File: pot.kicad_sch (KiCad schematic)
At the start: 8 parts, among them U25 LUM-1502-03_3.5mm_mono_vertic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, U26 LM358

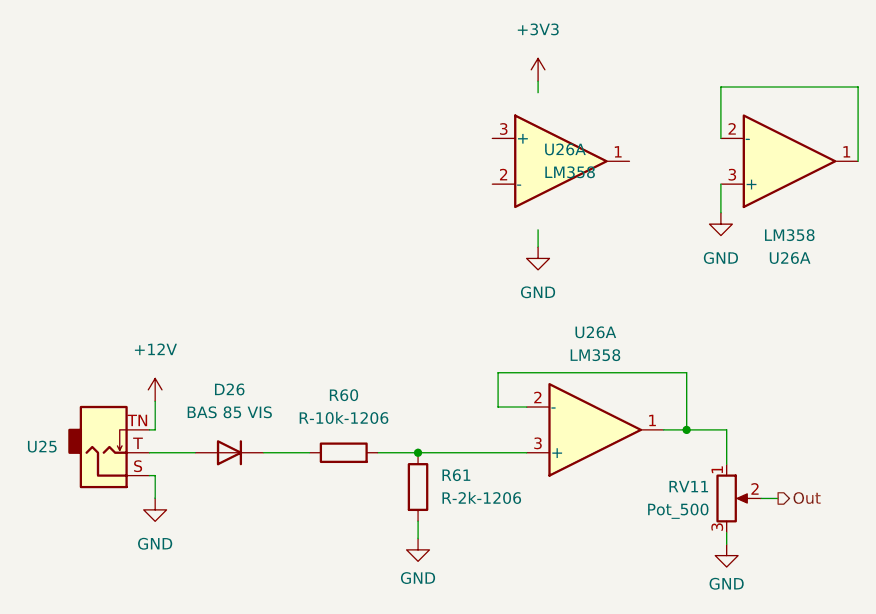
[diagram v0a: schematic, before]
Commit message: re-thinked the controls
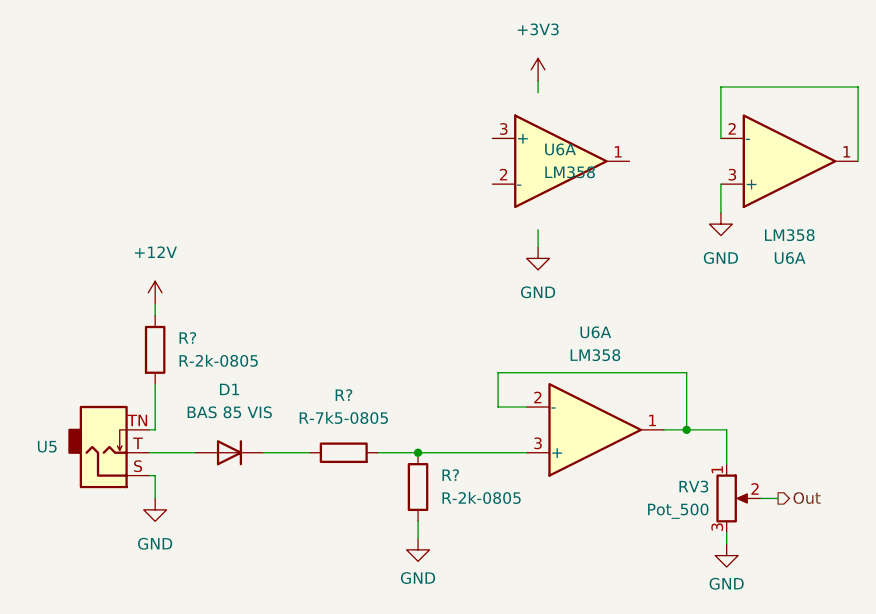
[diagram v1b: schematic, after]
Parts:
- removed R60: R-10k-1206, Resistor_SMD:R_1206_3216Metric_Pad1.30x1.75mm_HandSolder, symbol eurorack:R-10k-1206
- removed R61: R-2k-1206, Resistor_SMD:R_1206_3216Metric_Pad1.30x1.75mm_HandSolder, symbol eurorack:R-2k-1206
- added R? (x2): R-2k-0805, Resistor_SMD:R_0805_2012Metric, symbol eurorack:R-2k-0805
- added R?: R-7k5-0805, Resistor_SMD:R_0805_2012Metric, symbol eurorack:R-7k5-0805
- renumbered D26 to D1, RV11 to RV3, U25 to U5, U26 to U6
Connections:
- net +12V: now also R?.1; no longer U5.TN
- net GND: now also R?.2
- net at D1.2 (K): now also R?.1
- net at U6.3 (+): now also R?.1, R?.2
- new net: R?.2, U5.TN

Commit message: added some missing wires, whoopppssssz
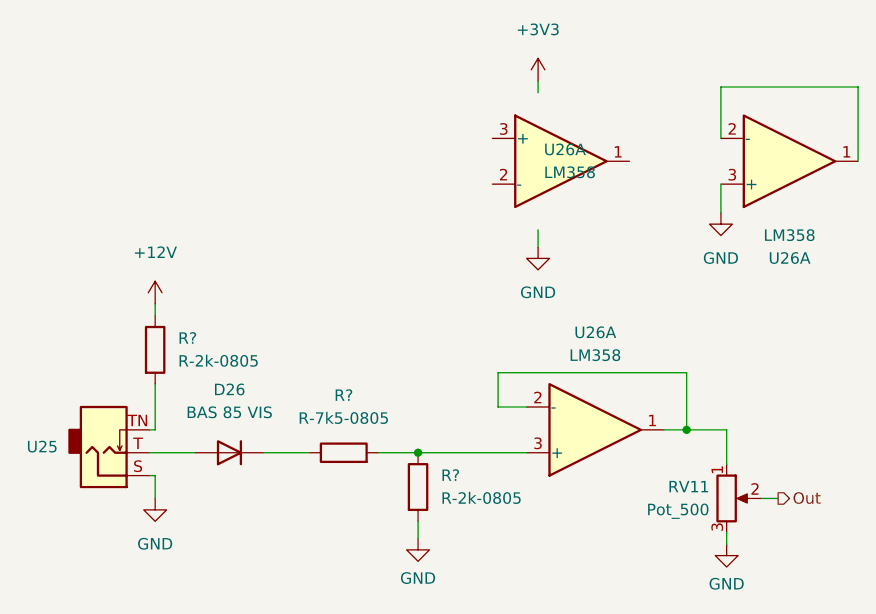
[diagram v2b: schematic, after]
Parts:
- renumbered D1 to D26, RV3 to RV11, U5 to U25, U6 to U26
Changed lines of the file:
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@@
+    (stroke (width 0) (type default) (color 0 0 0 0))
+  )
+  (wire (pts (xy 98.425 63.5) (xy 102.87 63.5))
+    (stroke (width 0) (type default) (color 0 0 0 0))
+  )
+  (wire (pts (xy 39.37 68.58) (xy 38.735 68.58))
+    (stroke (width 0) (type default) (color 0 0 0 0))
+  )
+  (wire (pts (xy 98.425 63.5) (xy 95.885 63.5))
+    (stroke (width 0) (type default) (color 0 0 0 0))
+  )
+  (wire (pts (xy 102.87 74.93) (xy 102.87 76.2))
+    (stroke (width 0) (type default) (color 0 0 0 0))
+  )
+  (wire (pts (xy 68.58 66.04) (xy 80.645 66.04))
+    (stroke (width 0) (type default) (color 0 0 0 0))
+  )
+  (wire (pts (xy 81.915 24.765) (xy 81.915 26.035))
+    (stroke (width 0) (type default) (color 0 0 0 0))
+  )
+  (wire (pts (xy 38.735 66.04) (xy 43.815 66.04))
+    (stroke (width 0) (type default) (color 0 0 0 0))
+  )
+  (wire (pts (xy 81.915 41.275) (xy 81.915 43.18))
+    (stroke (width 0) (type default) (color 0 0 0 0))
+  )
+  (wire (pts (xy 102.235 31.115) (xy 102.235 25.4))
+    (stroke (width 0) (type default) (color 0 0 0 0))
+  )
+  (wire (pts (xy 64.135 66.04) (xy 68.58 66.04))
+    (stroke (width 0) (type default) (color 0 0 0 0))
+  )
+  (wire (pts (xy 117.475 25.4) (xy 117.475 33.655))
+    (stroke (width 0) (type default) (color 0 0 0 0))
+  )
+  (wire (pts (xy 39.37 58.42) (xy 39.37 63.5))
+    (stroke (width 0) (type default) (color 0 0 0 0))
+  )
+  (wire (pts (xy 106.68 71.12) (xy 108.585 71.12))
     (stroke (width 0) (type default) (color 0 0 0 0))
   )
   (wire (pts (xy 39.37 49.53) (xy 39.37 50.8))
-    (stroke (width 0) (type default) (color 0 0 0 0))
-  )
-  (wire (pts (xy 98.425 63.5) (xy 102.87 63.5))
-    (stroke (width 0) (type default) (color 0 0 0 0))
-  )
-  (wire (pts (xy 39.37 68.58) (xy 38.735 68.58))
-    (stroke (width 0) (type default) (color 0 0 0 0))
-  )
-  (wire (pts (xy 98.425 63.5) (xy 95.885 63.5))
-    (stroke (width 0) (type default) (color 0 0 0 0))
-  )
-  (wire (pts (xy 102.87 74.93) (xy 102.87 76.2))
-    (stroke (width 0) (type default) (color 0 0 0 0))
-  )
-  (wire (pts (xy 68.58 66.04) (xy 80.645 66.04))
-    (stroke (width 0) (type default) (color 0 0 0 0))
-  )
-  (wire (pts (xy 81.915 24.765) (xy 81.915 26.035))
-    (stroke (width 0) (type default) (color 0 0 0 0))
-  )
-  (wire (pts (xy 38.735 66.04) (xy 43.815 66.04))
-    (stroke (width 0) (type default) (color 0 0 0 0))
-  )
-  (wire (pts (xy 81.915 41.275) (xy 81.915 43.18))
-    (stroke (width 0) (type default) (color 0 0 0 0))
-  )
-  (wire (pts (xy 102.235 31.115) (xy 102.235 25.4))
-    (stroke (width 0) (type default) (color 0 0 0 0))
-  )
-  (wire (pts (xy 64.135 66.04) (xy 68.58 66.04))
-    (stroke (width 0) (type default) (color 0 0 0 0))
-  )
-  (wire (pts (xy 117.475 25.4) (xy 117.475 33.655))
-    (stroke (width 0) (type default) (color 0 0 0 0))
-  )
-  (wire (pts (xy 39.37 58.42) (xy 39.37 63.5))
-    (stroke (width 0) (type default) (color 0 0 0 0))
-  )
-  (wire (pts (xy 106.68 71.12) (xy 108.585 71.12))
     (stroke (width 0) (type default) (color 0 0 0 0))
   )
@@
   (symbol (lib_id "eurorack:LUM-1502-03_3.5mm_mono_vertical_jack") (at 33.655 67.31 0) (mirror x)
     (in_bom yes) (on_board yes) (fields_autoplaced)
-    (property "Reference" "U5" (id 0) (at 28.575 65.4049 0)
+    (property "Reference" "U25" (id 0) (at 28.575 65.4049 0)
       (effects (font (size 1.27 1.27)) (justify right))
     )
@@
   (symbol (lib_id "power:+3V3") (at 81.915 24.765 0)
     (in_bom yes) (on_board yes) (fields_autoplaced)
-    (property "Reference" "#PWR038" (id 0) (at 81.915 28.575 0)
+    (property "Reference" "#PWR0121" (id 0) (at 81.915 28.575 0)
       (effects (font (size 1.27 1.27)) hide)
     )
@@
   (symbol (lib_id "eurorack:LM358") (at 88.265 63.5 0) (mirror x)
     (in_bom yes) (on_board yes) (fields_autoplaced)
-    (property "Reference" "U6" (id 0) (at 88.265 52.705 0))
+    (property "Reference" "U26" (id 0) (at 88.265 52.705 0))
     (property "Value" "LM358" (id 1) (at 88.265 55.245 0))
     (property "Footprint" "Package_SO:SO-8_3.9x4.9mm_P1.27mm" (id 2) (at 88.265 63.5 0)
@@
   (symbol (lib_id "power:GND") (at 39.37 71.12 0) (mirror y)
     (in_bom yes) (on_board yes) (fields_autoplaced)
-    (property "Reference" "#PWR036" (id 0) (at 39.37 77.47 0)
+    (property "Reference" "#PWR0119" (id 0) (at 39.37 77.47 0)
       (effects (font (size 1.27 1.27)) hide)
     )
@@
   (symbol (lib_id "eurorack:BAS 85 VIS") (at 47.625 66.04 180)
     (in_bom yes) (on_board yes) (fields_autoplaced)
-    (property "Reference" "D1" (id 0) (at 47.625 59.055 0))
+    (property "Reference" "D26" (id 0) (at 47.625 59.055 0))
     (property "Value" "BAS 85 VIS" (id 1) (at 47.625 61.595 0))
     (property "Footprint" "Diode_SMD:D_MiniMELF" (id 2) (at 47.625 61.595 0)
@@
   (symbol (lib_id "eurorack:LM358") (at 84.455 33.655 0)
     (in_bom yes) (on_board yes) (fields_autoplaced)
-    (property "Reference" "U6" (id 0) (at 82.55 32.3849 0)
+    (property "Reference" "U26" (id 0) (at 82.55 32.3849 0)
       (effects (font (size 1.27 1.27)) (justify left))
     )
@@
   (symbol (lib_id "power:GND") (at 102.87 76.2 0)
     (in_bom yes) (on_board yes) (fields_autoplaced)
-    (property "Reference" "#PWR041" (id 0) (at 102.87 82.55 0)
+    (property "Reference" "#PWR0124" (id 0) (at 102.87 82.55 0)
       (effects (font (size 1.27 1.27)) hide)
     )
@@
   (symbol (lib_id "power:GND") (at 81.915 43.18 0)
     (in_bom yes) (on_board yes) (fields_autoplaced)
-    (property "Reference" "#PWR039" (id 0) (at 81.915 49.53 0)
+    (property "Reference" "#PWR0122" (id 0) (at 81.915 49.53 0)
       (effects (font (size 1.27 1.27)) hide)
     )
@@
   (symbol (lib_id "eurorack:LM358") (at 109.855 33.655 0) (mirror x)
     (in_bom yes) (on_board yes) (fields_autoplaced)
-    (property "Reference" "U6" (id 0) (at 109.855 44.45 0))
+    (property "Reference" "U26" (id 0) (at 109.855 44.45 0))
     (property "Value" "LM358" (id 1) (at 109.855 41.91 0))
     (property "Footprint" "Package_SO:SO-8_3.9x4.9mm_P1.27mm" (id 2) (at 109.855 33.655 0)
@@
   (symbol (lib_id "eurorack:Pot_500") (at 102.87 71.12 0)
     (in_bom yes) (on_board yes) (fields_autoplaced)
-    (property "Reference" "RV3" (id 0) (at 100.965 69.8499 0)
+    (property "Reference" "RV11" (id 0) (at 100.965 69.8499 0)
       (effects (font (size 1.27 1.27)) (justify right))
     )
@@
   (symbol (lib_id "power:GND") (at 102.235 39.37 0)
     (in_bom yes) (on_board yes) (fields_autoplaced)
-    (property "Reference" "#PWR040" (id 0) (at 102.235 45.72 0)
+    (property "Reference" "#PWR0123" (id 0) (at 102.235 45.72 0)
       (effects (font (size 1.27 1.27)) hide)
     )
@@
   (symbol (lib_id "power:GND") (at 68.58 75.565 0)
     (in_bom yes) (on_board yes) (fields_autoplaced)
-    (property "Reference" "#PWR037" (id 0) (at 68.58 81.915 0)
-      (effects (font (size 1.27 1.27)) hide)
-    )
+    (property "Reference" "#PWR0120" (id 0) (at 68.58 81.915 0)
+      (effects (font (size 1.27 1.27)) hide)
+    )

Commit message: reannotated changed to LM324
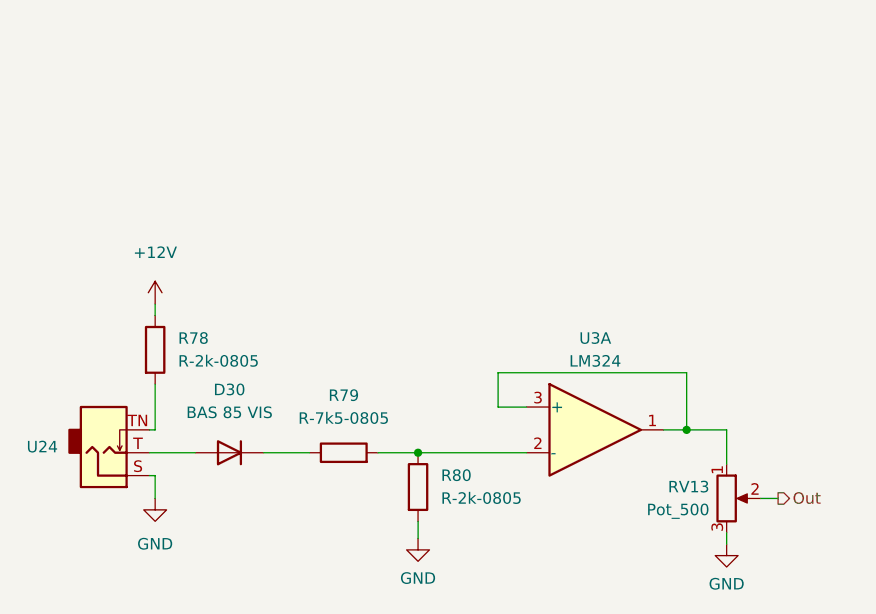
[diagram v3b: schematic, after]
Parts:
- removed U26 (x3): LM358, Package_SO:SO-8_3.9x4.9mm_P1.27mm, symbol eurorack:LM358
- added U3: LM324, Package_SO:SO-14_3.9x8.65mm_P1.27mm, symbol eurorack:LM324
- gave numbers to parts that had none: 3
- renumbered D26 to D30, RV11 to RV13, U25 to U24
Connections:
- net at RV13.1: now also U3.1, U3.3 (+)
- net at R79.2, R80.1: now also U3.2 (-)
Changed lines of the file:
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@@
-    (stroke (width 0) (type default) (color 0 0 0 0))
-  )
-  (wire (pts (xy 102.235 25.4) (xy 117.475 25.4))
-    (stroke (width 0) (type default) (color 0 0 0 0))
-  )
-  (wire (pts (xy 102.235 36.195) (xy 102.235 39.37))
     (stroke (width 0) (type default) (color 0 0 0 0))
   )
@@
     (stroke (width 0) (type default) (color 0 0 0 0))
   )
-  (wire (pts (xy 81.915 24.765) (xy 81.915 26.035))
-    (stroke (width 0) (type default) (color 0 0 0 0))
-  )
   (wire (pts (xy 38.735 66.04) (xy 43.815 66.04))
     (stroke (width 0) (type default) (color 0 0 0 0))
   )
-  (wire (pts (xy 81.915 41.275) (xy 81.915 43.18))
-    (stroke (width 0) (type default) (color 0 0 0 0))
-  )
-  (wire (pts (xy 102.235 31.115) (xy 102.235 25.4))
-    (stroke (width 0) (type default) (color 0 0 0 0))
-  )
   (wire (pts (xy 64.135 66.04) (xy 68.58 66.04))
-    (stroke (width 0) (type default) (color 0 0 0 0))
-  )
-  (wire (pts (xy 117.475 25.4) (xy 117.475 33.655))
     (stroke (width 0) (type default) (color 0 0 0 0))
   )
@@
   (symbol (lib_id "eurorack:LUM-1502-03_3.5mm_mono_vertical_jack") (at 33.655 67.31 0) (mirror x)
     (in_bom yes) (on_board yes) (fields_autoplaced)
-    (property "Reference" "U25" (id 0) (at 28.575 65.4049 0)
+    (property "Reference" "U24" (id 0) (at 28.575 65.4049 0)
       (effects (font (size 1.27 1.27)) (justify right))
     )
@@
     (pin "TN")
   )
-  (symbol (lib_id "power:+3V3") (at 81.915 24.765 0)
-    (in_bom yes) (on_board yes) (fields_autoplaced)
-    (property "Reference" "#PWR0121" (id 0) (at 81.915 28.575 0)
-      (effects (font (size 1.27 1.27)) hide)
-    )
-    (property "Value" "+3V3" (id 1) (at 81.915 19.05 0))
-    (property "Footprint" "" (id 2) (at 81.915 24.765 0)
-      (effects (font (size 1.27 1.27)) hide)
-    )
-    (property "Datasheet" "" (id 3) (at 81.915 24.765 0)
-      (effects (font (size 1.27 1.27)) hide)
-    )
-    (pin "1")
-  )
-  (symbol (lib_id "eurorack:LM358") (at 88.265 63.5 0) (mirror x)
-    (in_bom yes) (on_board yes) (fields_autoplaced)
-    (property "Reference" "U26" (id 0) (at 88.265 52.705 0))
-    (property "Value" "LM358" (id 1) (at 88.265 55.245 0))
-    (property "Footprint" "Package_SO:SO-8_3.9x4.9mm_P1.27mm" (id 2) (at 88.265 63.5 0)
-      (effects (font (size 1.27 1.27)) hide)
-    )
-    (property "Datasheet" "https://www.reichelt.com/at/en/operational-amplifier-dual-1mhz-so-8-lm-358-am-p187541.html?&trstct=pos_0&nbc=1" (id 3) (at 88.265 63.5 0)
-      (effects (font (size 1.27 1.27)) hide)
-    )
-    (pin "1")
-    (pin "2")
-    (pin "3")
+  (symbol (lib_id "eurorack:LM324") (at 88.265 63.5 0)
+    (in_bom yes) (on_board yes) (fields_autoplaced)
+    (property "Reference" "U3" (id 0) (at 88.265 53.34 0))
+    (property "Value" "LM324" (id 1) (at 88.265 55.88 0))
+    (property "Footprint" "Package_SO:SO-14_3.9x8.65mm_P1.27mm" (id 2) (at 86.995 60.96 0)
+      (effects (font (size 1.27 1.27)) hide)
+    )
+    (property "Datasheet" "http://www.ti.com/lit/ds/symlink/lm2902-n.pdf" (id 3) (at 89.535 58.42 0)
+      (effects (font (size 1.27 1.27)) hide)
+    )
+    (pin "12")
+    (pin "13")
+    (pin "14")
   )
   (symbol (lib_id "power:GND") (at 39.37 71.12 0) (mirror y)
     (in_bom yes) (on_board yes) (fields_autoplaced)
-    (property "Reference" "#PWR0119" (id 0) (at 39.37 77.47 0)
+    (property "Reference" "#PWR0112" (id 0) (at 39.37 77.47 0)
       (effects (font (size 1.27 1.27)) hide)
     )
@@
   (symbol (lib_id "eurorack:BAS 85 VIS") (at 47.625 66.04 180)
     (in_bom yes) (on_board yes) (fields_autoplaced)
-    (property "Reference" "D26" (id 0) (at 47.625 59.055 0))
+    (property "Reference" "D30" (id 0) (at 47.625 59.055 0))
     (property "Value" "BAS 85 VIS" (id 1) (at 47.625 61.595 0))
     (property "Footprint" "Diode_SMD:D_MiniMELF" (id 2) (at 47.625 61.595 0)
@@
     (pin "2")
   )
-  (symbol (lib_id "eurorack:LM358") (at 84.455 33.655 0)
-    (in_bom yes) (on_board yes) (fields_autoplaced)
-    (property "Reference" "U26" (id 0) (at 82.55 32.3849 0)
-      (effects (font (size 1.27 1.27)) (justify left))
-    )
-    (property "Value" "LM358" (id 1) (at 82.55 34.9249 0)
-      (effects (font (size 1.27 1.27)) (justify left))
-    )
-    (property "Footprint" "Package_SO:SO-8_3.9x4.9mm_P1.27mm" (id 2) (at 84.455 33.655 0)
-      (effects (font (size 1.27 1.27)) hide)
-    )
-    (property "Datasheet" "https://www.reichelt.com/at/en/operational-amplifier-dual-1mhz-so-8-lm-358-am-p187541.html?&trstct=pos_0&nbc=1" (id 3) (at 84.455 33.655 0)
-      (effects (font (size 1.27 1.27)) hide)
-    )
-    (pin "4")
-    (pin "8")
-  )
   (symbol (lib_id "power:GND") (at 102.87 76.2 0)
     (in_bom yes) (on_board yes) (fields_autoplaced)
-    (property "Reference" "#PWR0124" (id 0) (at 102.87 82.55 0)
+    (property "Reference" "#PWR0114" (id 0) (at 102.87 82.55 0)
       (effects (font (size 1.27 1.27)) hide)
     )
@@
     (pin "1")
   )
-  (symbol (lib_id "power:GND") (at 81.915 43.18 0)
-    (in_bom yes) (on_board yes) (fields_autoplaced)
-    (property "Reference" "#PWR0122" (id 0) (at 81.915 49.53 0)
-      (effects (font (size 1.27 1.27)) hide)
-    )
-    (property "Value" "GND" (id 1) (at 81.915 48.26 0))
-    (property "Footprint" "" (id 2) (at 81.915 43.18 0)
-      (effects (font (size 1.27 1.27)) hide)
-    )
-    (property "Datasheet" "" (id 3) (at 81.915 43.18 0)
-      (effects (font (size 1.27 1.27)) hide)
-    )
-    (pin "1")
-  )
-  (symbol (lib_id "eurorack:LM358") (at 109.855 33.655 0) (mirror x)
-    (in_bom yes) (on_board yes) (fields_autoplaced)
-    (property "Reference" "U26" (id 0) (at 109.855 44.45 0))
-    (property "Value" "LM358" (id 1) (at 109.855 41.91 0))
-    (property "Footprint" "Package_SO:SO-8_3.9x4.9mm_P1.27mm" (id 2) (at 109.855 33.655 0)
-      (effects (font (size 1.27 1.27)) hide)
-    )
-    (property "Datasheet" "https://www.reichelt.com/at/en/operational-amplifier-dual-1mhz-so-8-lm-358-am-p187541.html?&trstct=pos_0&nbc=1" (id 3) (at 109.855 33.655 0)
-      (effects (font (size 1.27 1.27)) hide)
-    )
-    (pin "5")
-    (pin "6")
-    (pin "7")
-  )
   (symbol (lib_id "eurorack:Pot_500") (at 102.87 71.12 0)
     (in_bom yes) (on_board yes) (fields_autoplaced)
-    (property "Reference" "RV11" (id 0) (at 100.965 69.8499 0)
+    (property "Reference" "RV13" (id 0) (at 100.965 69.8499 0)
       (effects (font (size 1.27 1.27)) (justify right))
     )
@@
   (symbol (lib_id "eurorack:R-2k-0805") (at 68.58 69.85 0)
     (in_bom yes) (on_board yes) (fields_autoplaced)
-    (property "Reference" "R?" (id 0) (at 71.12 68.5799 0)
+    (property "Reference" "R80" (id 0) (at 71.12 68.5799 0)
       (effects (font (size 1.27 1.27)) (justify left))
     )
@@
   (symbol (lib_id "eurorack:R-2k-0805") (at 39.37 54.61 0)
     (in_bom yes) (on_board yes) (fields_autoplaced)
-    (property "Reference" "R?" (id 0) (at 41.91 53.3399 0)
+    (property "Reference" "R78" (id 0) (at 41.91 53.3399 0)
       (effects (font (size 1.27 1.27)) (justify left))
     )
@@
     (pin "2")
   )
-  (symbol (lib_id "power:GND") (at 102.235 39.37 0)
-    (in_bom yes) (on_board yes) (fields_autoplaced)
-    (property "Reference" "#PWR0123" (id 0) (at 102.235 45.72 0)
-      (effects (font (size 1.27 1.27)) hide)
-    )
-    (property "Value" "GND" (id 1) (at 102.235 44.45 0))
-    (property "Footprint" "" (id 2) (at 102.235 39.37 0)
-      (effects (font (size 1.27 1.27)) hide)
-    )
-    (property "Datasheet" "" (id 3) (at 102.235 39.37 0)
-      (effects (font (size 1.27 1.27)) hide)
-    )
-    (pin "1")
-  )
   (symbol (lib_id "power:+12V") (at 39.37 49.53 0)
     (in_bom yes) (on_board yes) (fields_autoplaced)
-    (property "Reference" "#PWR?" (id 0) (at 39.37 53.34 0)
+    (property "Reference" "#PWR0111" (id 0) (at 39.37 53.34 0)
       (effects (font (size 1.27 1.27)) hide)
     )
@@
   (symbol (lib_id "power:GND") (at 68.58 75.565 0)
     (in_bom yes) (on_board yes) (fields_autoplaced)
-    (property "Reference" "#PWR0120" (id 0) (at 68.58 81.915 0)
+    (property "Reference" "#PWR0113" (id 0) (at 68.58 81.915 0)
       (effects (font (size 1.27 1.27)) hide)
     )
@@
   (symbol (lib_id "eurorack:R-7k5-0805") (at 60.325 66.04 90)
     (in_bom yes) (on_board yes) (fields_autoplaced)
-    (property "Reference" "R?" (id 0) (at 60.325 59.69 90))
+    (property "Reference" "R79" (id 0) (at 60.325 59.69 90))
     (property "Value" "R-7k5-0805" (id 1) (at 60.325 62.23 90))
     (property "Footprint" "Resistor_SMD:R_0805_2012Metric" (id 2) (at 60.325 67.818 90)
